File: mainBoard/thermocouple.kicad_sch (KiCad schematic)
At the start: 18 parts, among them J10 4DB-P108-02, U5 OPA333AIDCKT, U7 DS18B20+

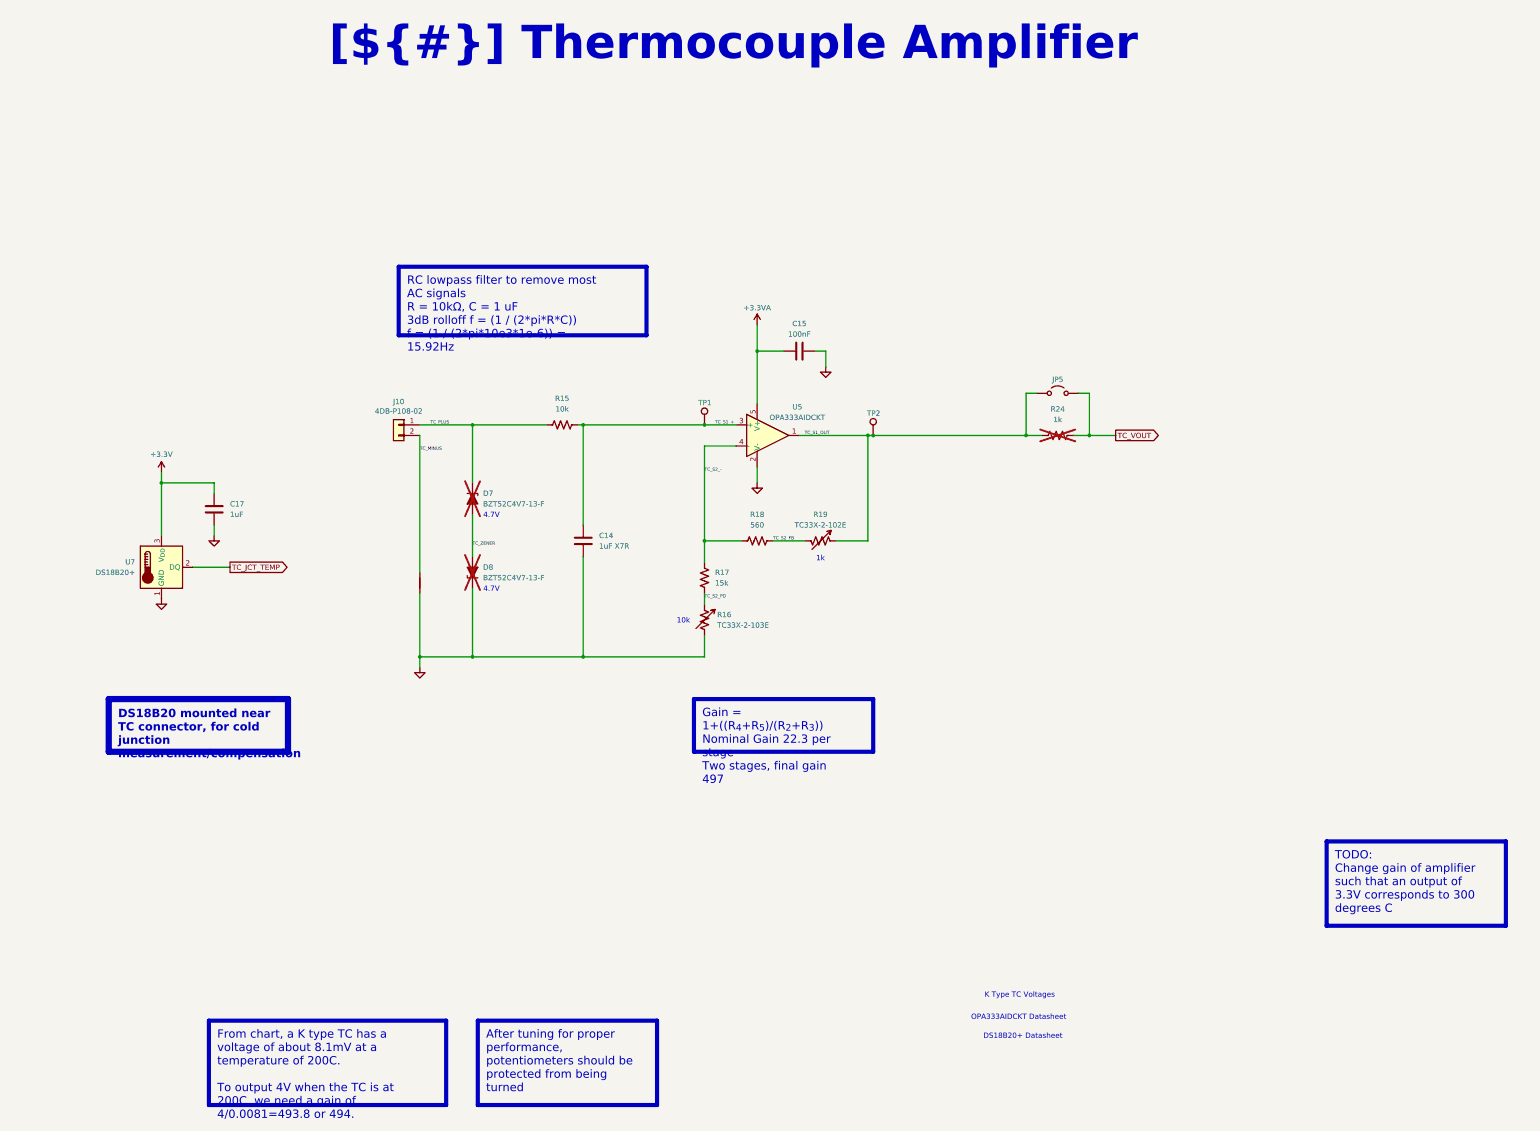
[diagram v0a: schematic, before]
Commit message: Schematic Capture should be complete, ready for PCB
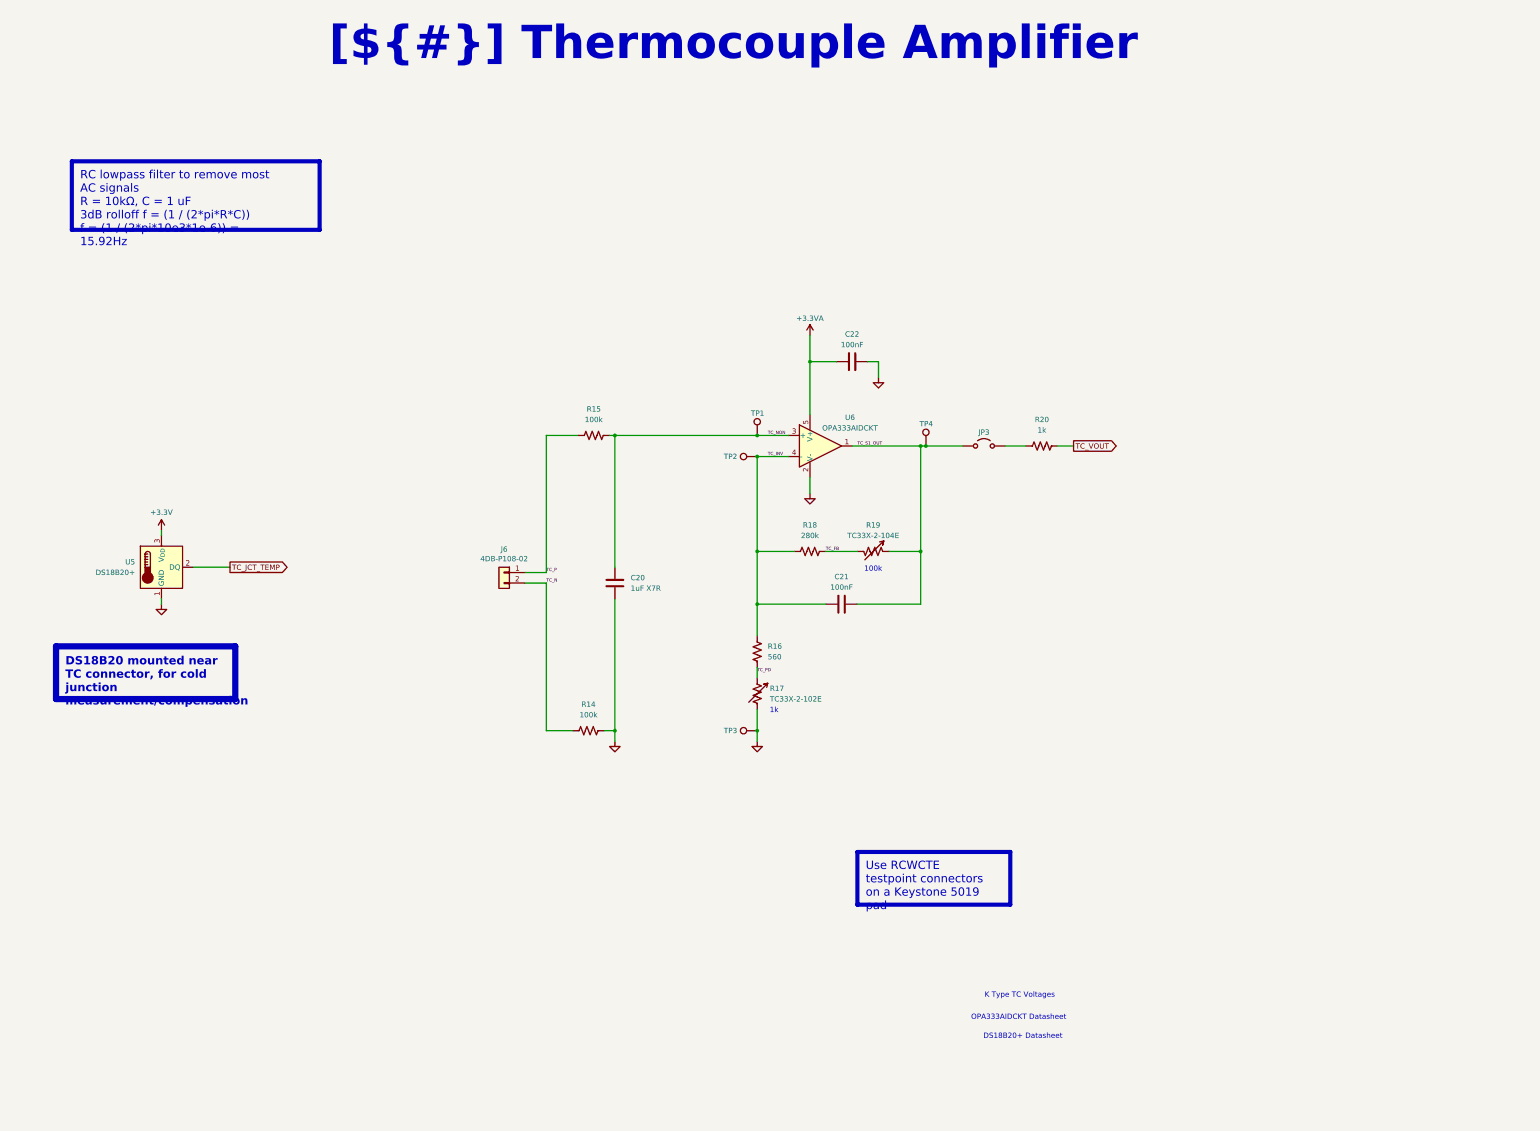
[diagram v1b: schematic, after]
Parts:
- removed C17: 1uF, Capacitor_SMD:C_0805_2012Metric_Pad1.18x1.45mm_HandSolder, symbol Device:C
- removed D7, D8: BZT52C4V7-13-F, Diode_SMD:D_SOD-123, symbol Device:D_Zener_Filled
- removed NT1: NetTie_2, NetTie:NetTie-2_SMD_Pad0.5mm, symbol Device:NetTie_2
- added C21: 100nF, Capacitor_SMD:C_0805_2012Metric_Pad1.18x1.45mm_HandSolder, symbol Device:C
- added R14: 100k, Resistor_SMD:R_0603_1608Metric_Pad0.98x0.95mm_HandSolder, symbol Device:R_US
- added TP2, TP3: TestPoint, TestPoint:TestPoint_Keystone_5019_Miniature, symbol Connector:TestPoint
- R15: value 10k -> 100k
- R16: renamed from R17; value 15k -> 560
- R17: renamed from R16; value TC33X-2-103E -> TC33X-2-102E
- R18: value 560 -> 280k
- R19: value TC33X-2-102E -> TC33X-2-104E
- R20: renamed from R24; now fitted
- TP1: footprint Connector_PinHeader_2.54mm:PinHeader_1x01_P2.54mm_Vertical -> TestPoint:TestPoint_Keystone_5019_Miniature
- TP4: renamed from TP2; footprint Connector_PinHeader_2.54mm:PinHeader_1x01_P2.54mm_Vertical -> TestPoint:TestPoint_Keystone_5019_Miniature
- renumbered C14 to C20, C15 to C22, J10 to J6, JP5 to JP3, U7 to U5, U5 to U6
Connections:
- net GND: now also R14.2, TP3.1
- net TC_S1_OUT: now also C21.2; no longer R20.1
- net TC_VOUT: no longer JP3.2 (B)
- net TC_MINUS renamed TC_N
- net TC_N: now also R14.1
- net TC_PLUS renamed TC_P
- net TC_S1_+ renamed TC_NON
- net TC_S2_- renamed TC_INV
- net TC_INV: now also C21.1, TP2.1
- net TC_S2_FB renamed TC_FB
- net TC_S2_PD renamed TC_PD
- new net: JP3.2 (B), R20.1
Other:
- note added: "100k"
- note removed: "10k"
- note removed: "4.7V"
- moved on the sheet: C20, C22, J6, JP3, R15, R16, R17, R18, R19, TP1, TP4, U6

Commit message: tweak schematic for changes from 6-17-2026
major structural changes, see daily note from obsidian
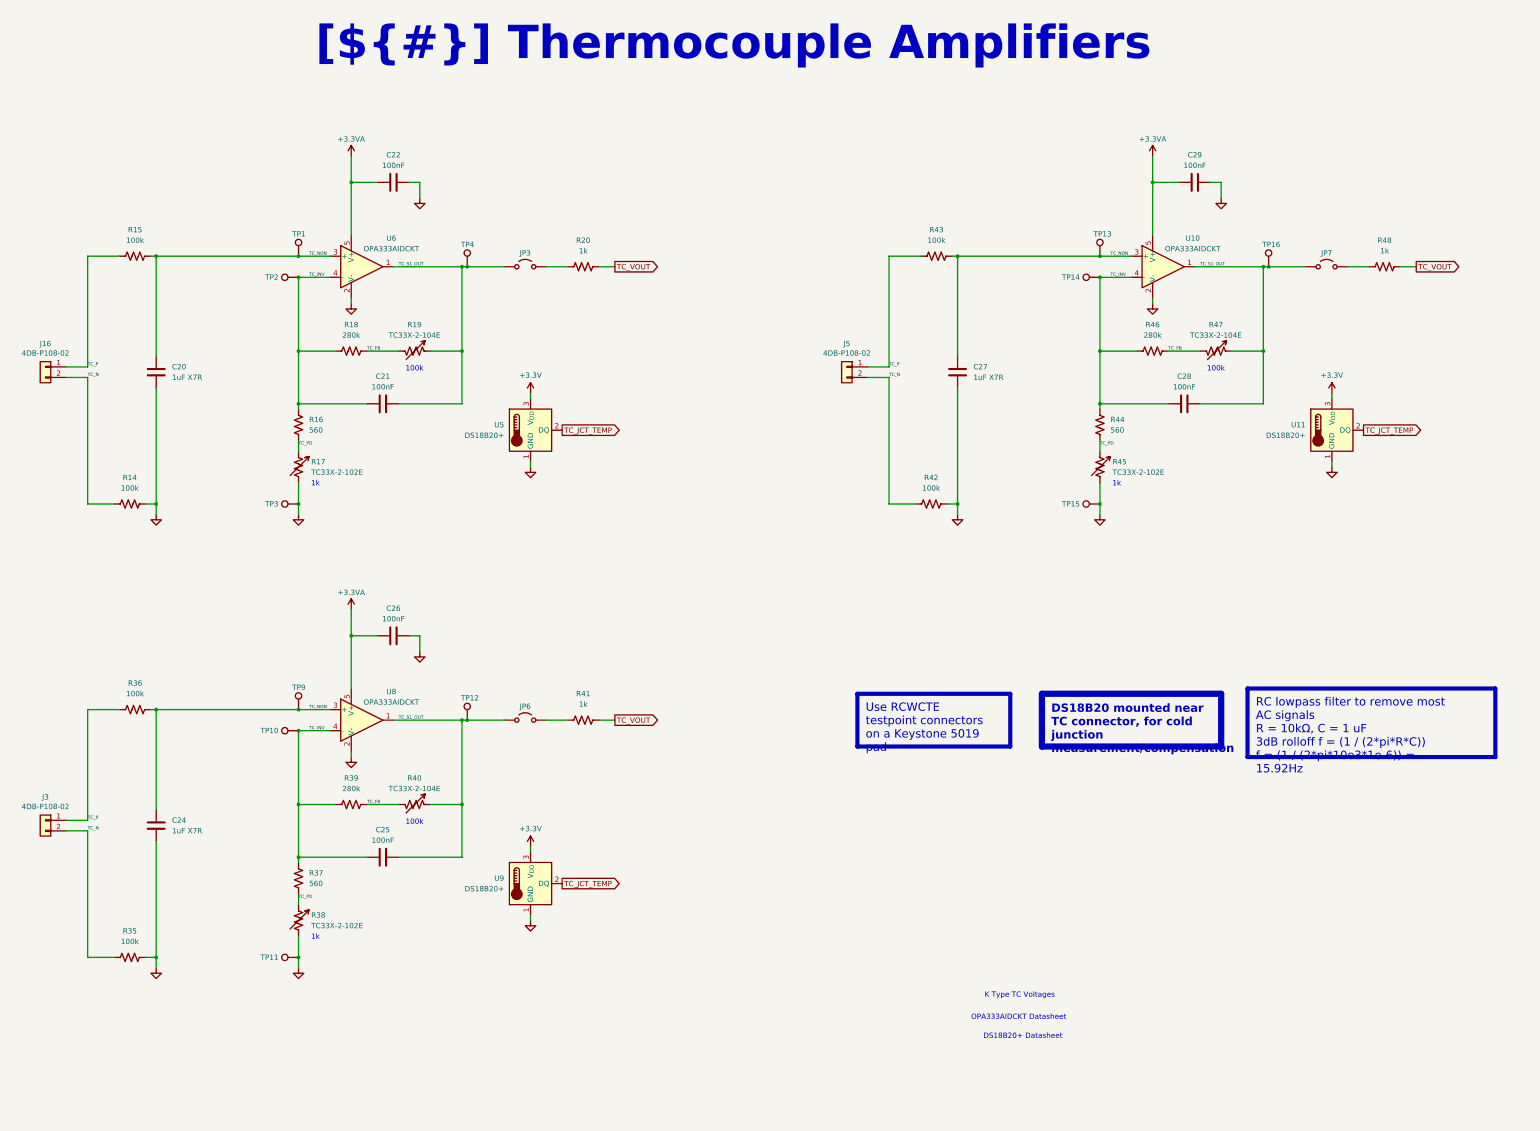
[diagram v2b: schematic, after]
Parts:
- added C24, C27: 1uF X7R, Capacitor_SMD:C_0603_1608Metric_Pad1.08x0.95mm_HandSolder, symbol Device:C
- added C25, C26, C28, C29: 100nF, Capacitor_SMD:C_0805_2012Metric_Pad1.18x1.45mm_HandSolder, symbol Device:C
- added J3, J5: 4DB-P108-02, 4DB_P108_02:CONN_4DB-P108-02_TEC, symbol Connector_Generic:Conn_01x02
- added JP6, JP7: Jumper_2_Open, Jumper:SolderJumper-2_P1.3mm_Open_TrianglePad1.0x1.5mm, symbol Jumper:Jumper_2_Open
- added R35, R36, R42, R43: 100k, Resistor_SMD:R_0603_1608Metric_Pad0.98x0.95mm_HandSolder, symbol Device:R_US
- added R37, R44: 560, Resistor_SMD:R_0603_1608Metric_Pad0.98x0.95mm_HandSolder, symbol Device:R_US
- added R38, R45: TC33X-2-102E, Potentiometer_SMD:Potentiometer_Bourns_TC33X_Vertical, symbol Device:R_Variable_US
- added R39, R46: 280k, Resistor_SMD:R_0603_1608Metric_Pad0.98x0.95mm_HandSolder, symbol Device:R_US
- added R40, R47: TC33X-2-104E, Potentiometer_SMD:Potentiometer_Bourns_TC33X_Vertical, symbol Device:R_Variable_US
- added R41, R48: 1k, Resistor_SMD:R_0603_1608Metric_Pad0.98x0.95mm_HandSolder, symbol Device:R_US
- added TP10, TP11, TP12, TP13, TP14, TP15, TP16, TP9: TestPoint, TestPoint:TestPoint_Keystone_5019_Miniature, symbol Connector:TestPoint
- added U10, U8: OPA333AIDCKT, Package_SO:SOIC-8_3.9x4.9mm_P1.27mm, symbol Amplifier_Operational:OPA333xxDBV
- added U11, U9: DS18B20+, Package_TO_SOT_THT:TO-92_Inline, symbol Sensor_Temperature:DS18B20
- renumbered J6 to J16
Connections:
- net +3.3V: now also U11.3 (V_{DD}), U9.3 (V_{DD})
- net +3.3VA: now also C26.1, C29.1, U10.5 (V+), U8.5 (V+)
- net GND: now also C24.2, C26.2, C27.2, C29.2, R35.2, R38.2, R42.2, R45.2, TP11.1, TP15.1, U10.2 (V-), U11.1 (GND), U8.2 (V-), U9.1 (GND)
- net TC_FB: now also R39.2, R40.2, R46.2, R47.2
- net TC_INV: now also C25.1, C28.1, R37.1, R39.1, R44.1, R46.1, TP10.1, TP14.1, U10.4 (-), U8.4 (-)
- net TC_JCT_TEMP: now also U11.2 (DQ), U9.2 (DQ)
- net TC_N: now also J3.2 (Pin_2), J5.2 (Pin_2), R35.1, R42.1
- net TC_NON: now also C24.1, C27.1, R36.2, R43.2, TP13.1, TP9.1, U10.3 (+), U8.3 (+)
- net TC_P: now also J3.1 (Pin_1), J5.1 (Pin_1), R36.1, R43.1
- net TC_PD: now also R37.2, R38.1, R44.2, R45.1
- net TC_S1_OUT: now also C25.2, C28.2, JP6.1 (A), JP7.1 (A), R40.1, R47.1, TP12.1, TP16.1, U10.1, U8.1
- net TC_VOUT: now also R41.2, R48.2
- new net: JP7.2 (B), R48.1
- new net: JP6.2 (B), R41.1
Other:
- title: Thermocouple Amplifier -> Thermocouple Amplifiers
- moved on the sheet: C20, C21, C22, J16, JP3, R14, R15, R16, R17, R18, R19, R20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

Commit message: working on pcb layout after bringing in work from laptop
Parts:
- removed C24, C27: 1uF X7R, Capacitor_SMD:C_0603_1608Metric_Pad1.08x0.95mm_HandSolder, symbol Device:C
- removed C25, C26, C29: 100nF, Capacitor_SMD:C_0805_2012Metric_Pad1.18x1.45mm_HandSolder, symbol Device:C
- removed J3: 4DB-P108-02, 4DB_P108_02:CONN_4DB-P108-02_TEC, symbol Connector_Generic:Conn_01x02
- removed R36, R43: 100k, Resistor_SMD:R_0603_1608Metric_Pad0.98x0.95mm_HandSolder, symbol Device:R_US
- removed R37: 560, Resistor_SMD:R_0603_1608Metric_Pad0.98x0.95mm_HandSolder, symbol Device:R_US
- removed R38: TC33X-2-102E, Potentiometer_SMD:Potentiometer_Bourns_TC33X_Vertical, symbol Device:R_Variable_US
- removed R40, R47: TC33X-2-104E, Potentiometer_SMD:Potentiometer_Bourns_TC33X_Vertical, symbol Device:R_Variable_US
- removed R48: 1k, Resistor_SMD:R_0603_1608Metric_Pad0.98x0.95mm_HandSolder, symbol Device:R_US
- removed TP11: TestPoint, TestPoint:TestPoint_Keystone_5019_Miniature, symbol Connector:TestPoint
- removed U10, U8: OPA333AIDCKT, Package_SO:SOIC-8_3.9x4.9mm_P1.27mm, symbol Amplifier_Operational:OPA333xxDBV
- removed U9: DS18B20+, Package_TO_SOT_THT:TO-92_Inline, symbol Sensor_Temperature:DS18B20
- added C30, C32, C36, C37: 100nF, Capacitor_SMD:C_0805_2012Metric_Pad1.18x1.45mm_HandSolder, symbol Device:C
- added C33, C34, C38: 10uF, Capacitor_SMD:C_0603_1608Metric_Pad1.08x0.95mm_HandSolder, symbol Device:C
- added C35: 1uF X7R, Capacitor_SMD:C_0603_1608Metric_Pad1.08x0.95mm_HandSolder, symbol Device:C
- added J6: 4DB-P108-02, 4DB_P108_02:CONN_4DB-P108-02_TEC, symbol Connector_Generic:Conn_01x02
- added R27, R29, R40: 100k, Resistor_SMD:R_0603_1608Metric_Pad0.98x0.95mm_HandSolder, symbol Device:R_US
- added R32: 560, Resistor_SMD:R_0603_1608Metric_Pad0.98x0.95mm_HandSolder, symbol Device:R_US
- added R33, R43: TC33X-2-102E, Potentiometer_SMD:Potentiometer_Bourns_TC33X_Vertical, symbol Device:R_Variable_US
- added R37: TC33X-2-104E, Potentiometer_SMD:Potentiometer_Bourns_TC33X_Vertical, symbol Device:R_Variable_US
- added TP8: TestPoint, TestPoint:TestPoint_Keystone_5019_Miniature, symbol Connector:TestPoint
- added U12, U9: OPA333AIDCKT, Package_SO:SOIC-8_3.9x4.9mm_P1.27mm, symbol Amplifier_Operational:OPA333xxDBV
- added U13: DS18B20+, Package_TO_SOT_THT:TO-92_Inline, symbol Sensor_Temperature:DS18B20
- C28: value 100nF -> 1uF X7R; footprint Capacitor_SMD:C_0805_2012Metric_Pad1.18x1.45mm_HandSolder -> Capacitor_SMD:C_0603_1608Metric_Pad1.08x0.95mm_HandSolder
- R35: value 100k -> 280k
- R39, R46: value 280k -> 1k
- R41: value 1k -> 100k
- R42: value 100k -> 560
- R44: value 560 -> 280k
- R45: value TC33X-2-102E -> TC33X-2-104E
- renumbered C20 to C27, C21 to C29, C22 to C31, J16 to J4, JP3 to JP5, R14 to R26, R15 to R28, R16 to R30, R17 to R31, R18 to R34, R19 to R36, R20 to R38, TP4 to TP11, TP1 to TP5, TP2 to TP6, TP3 to TP7, U5 to U10, U6 to U8
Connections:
- net +3.3V: now also U13.3 (V_{DD})
- net +3.3VA: now also C32.1, C37.1, U12.5 (V+), U9.5 (V+)
- net GND: now also C28.2, TP10.1, C32.2, C33.2, C34.2, C35.2, C37.2, C38.2, R27.2, R33.2, R40.2, R43.2, U12.2 (V-), U13.1 (GND), U9.2 (V-); no longer R35.2, R42.2, R45.2
- net TC3_ADC_RC: now reaches JP7.2 (B)
- net TC3_ADC_RC: now also R46.1
- net TC1_ADC_RC: now reaches JP5.2 (B), R38.1
- net TC2_ADC_RC: now reaches JP6.2 (B)
- net TC2_ADC_RC: now also R39.1; no longer R41.1
- net TC_FB renamed TC1_FB
- net TC1_FB: no longer R39.2, R46.2
- removed net TC_INV: C28.1, C29.1, R30.1, R34.1, R39.1, R44.1, R46.1, TP10.1, TP14.1, TP6.1, U8.4 (-)
- net TC_JCT_TEMP renamed TC1_CJ_TEMP
- net TC1_CJ_TEMP: no longer U11.2 (DQ)
- removed net TC_N: J4.2 (Pin_2), J5.2 (Pin_2), R26.1, R35.1, R42.1
- net TC_NON renamed TC1_AFE_NON
- net TC1_AFE_NON: no longer TP13.1, TP9.1
- removed net TC_P: J4.1 (Pin_1), J5.1 (Pin_1), R28.1
- net TC_PD renamed TC1_AFE_PD
- net TC1_AFE_PD: no longer R44.2, R45.1
- net TC_S1_OUT renamed TC1_AFE_OUT
- net TC1_AFE_OUT: no longer C28.2, JP6.1 (A), JP7.1 (A), TP12.1, TP16.1
- net TC_VOUT renamed TC1_ADC
- net TC1_ADC: now also C33.1; no longer R41.2
- new net TC1_AFE_INV: C29.1, R30.1, R34.1, TP6.1, U8.4 (-)
- new net TC1_N: J4.1 (Pin_1), R26.1
- new net TC1_P: J4.2 (Pin_2), R28.1
- new net TC2_ADC: C34.1, R39.2
- new net TC2_AFE_INV: C30.1, R32.1, R35.1, TP9.1, U9.4 (-)
- new net TC2_AFE_NON: C28.1, R29.2, TP8.1, U9.3 (+)
- new net TC2_AFE_OUT: C30.2, JP6.1 (A), R37.1, TP12.1, U9.1
- new net TC2_AFE_PD: R32.2, R33.1
- new net TC2_CJ_TEMP: U11.2 (DQ)
- new net TC2_FB: R35.2, R37.2
- new net TC2_N: J5.2 (Pin_2), R27.1
- new net TC2_P: J5.1 (Pin_1), R29.1
- new net TC3_ADC: C38.1, R46.2
- new net TC3_AFE_INV: C36.1, R42.1, R44.1, TP14.1, U12.4 (-)
- new net TC3_AFE_NON: C35.1, R41.2, TP13.1, U12.3 (+)
- new net TC3_AFE_OUT: C36.2, JP7.1 (A), R45.1, TP16.1, U12.1
- new net TC3_AFE_PD: R42.2, R43.1
- new net TC3_CJ_TEMP: U13.2 (DQ)
- new net TC3_FB: R44.2, R45.2
- new net TC3_N: J6.2 (Pin_2), R40.1
- new net TC3_P: J6.1 (Pin_1), R41.1
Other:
- moved on the sheet: C27, C29, C31, J4, JP5, R26, R28, R30, R31, R34, R36, R38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
